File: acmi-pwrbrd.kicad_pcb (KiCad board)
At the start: 2 copper layers, 60 x 140 mm, 25 parts, among them J1 430450402, J10 3-641215-8, J2 430450402, J3 430451202, J4 430451202, J5 430450402

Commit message: Finish routing
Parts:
- removed J10: 3-641215-8, myparts:TE_3-641215-8
- added J6: 39289108, myparts:MOLEX_39289108, F.Cu at (196.5, 124.2)
- added J7: 430451202, myparts:CONN_SD-43045-001_12_MOL, F.Cu at (157.6, 83.2)
- D3: value GREEN -> ~
- moved J5 29.9 mm to (157.6, 55.2)
- moved MT1 25.0 mm to (155.0, 40.0)
- moved MT2 25.0 mm to (205.0, 40.0)
- moved J1 2.56 mm to (157.6, 158.0)
- moved J2 2.56 mm to (157.6, 175.0)
- moved J3 2.56 mm to (157.6, 111.8)
- moved J4 2.56 mm to (157.6, 140.0)
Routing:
- net +12V: track 0.00 -> 242.9 mm, vias 0 -> 4
- net +15V: track 0.00 -> 208.2 mm, vias 0 -> 3
- net -15V: track 0.00 -> 202.8 mm, vias 0 -> 3
- net -5V: track 0.00 -> 191.1 mm, vias 0 -> 4
- net +5V: track 0.00 -> 182.4 mm, vias 0 -> 2
- net GND: track 0.00 -> 9.47 mm, vias 0 -> 5
- net Net-(D3-A): track 0.00 -> 3.26 mm
- net Net-(D5-A): track 0.00 -> 3.24 mm
- net Net-(D4-K): track 0.00 -> 3.24 mm
- net Net-(D2-A): track 0.00 -> 3.24 mm
- net Net-(D1-K): track 0.00 -> 3.24 mm
- added copper zone on B.Cu, net GND
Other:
- board size 60 x 140 mm -> 60 x 165 mm
- board text added: "ACMI-2 Power Distribution Board"
- board text added: "J. Mead 2-24-25 Rev 1"

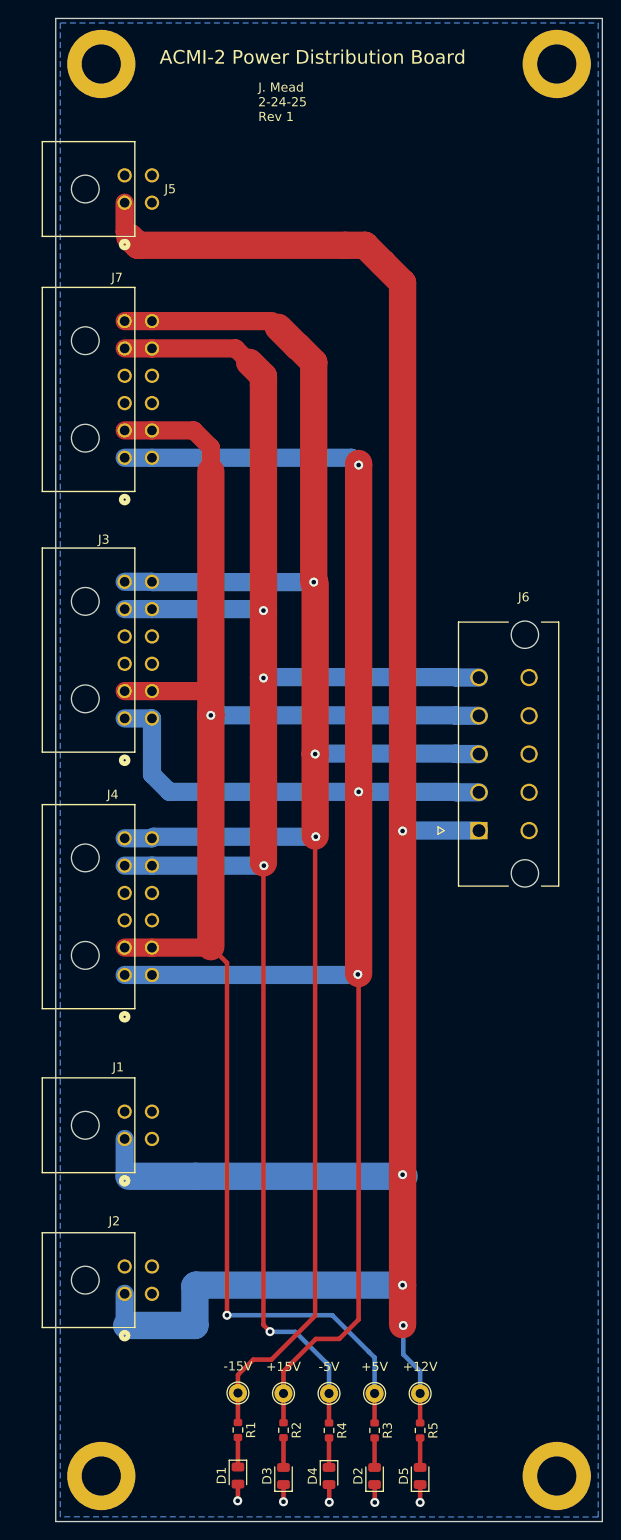
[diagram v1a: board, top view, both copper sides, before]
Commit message: Added 12VB, testpoints, cable harness
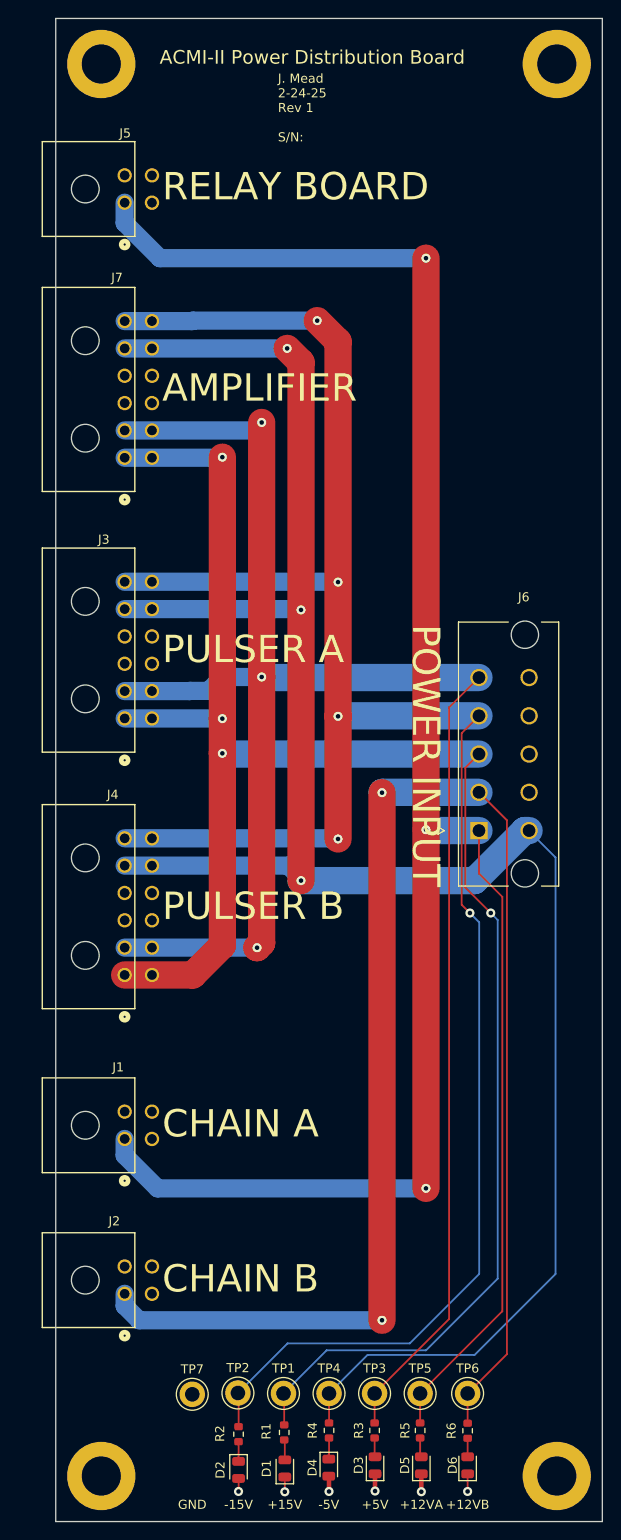
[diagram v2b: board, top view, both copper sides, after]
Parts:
- added D6: ~, LED_SMD:LED_0805_2012Metric, F.Cu at (195.2, 193.8)
- added R6: 895, Resistor_SMD:R_0603_1608Metric, F.Cu at (195.2, 190.0)
- added TP6: +12VB, TestPoint:TestPoint_Keystone_5005-5009_Compact, F.Cu at (195.2, 185.9)
- added TP7: GND, TestPoint:TestPoint_Keystone_5005-5009_Compact, F.Cu at (165.0, 186.0)
- TP1, TP2, TP3, TP4: footprint TestPoint:TestPoint_THTPad_D2.0mm_Drill1.0mm -> TestPoint:TestPoint_Keystone_5005-5009_Compact
- TP5: value +12V -> +12VA; footprint TestPoint:TestPoint_THTPad_D2.0mm_Drill1.0mm -> TestPoint:TestPoint_Keystone_5005-5009_Compact
- moved D2 14.9 mm to (170.1, 194.3), turned to -90 degrees
- moved D3 10.1 mm to (185.1, 193.8)
- moved D1 5.20 mm to (175.1, 194.2), turned to 90 degrees
- moved R1 5.09 mm to (175.1, 190.2)
- moved R2 4.95 mm to (170.1, 190.4)
- moved D5 1.18 mm to (190.1, 193.8)
- moved D4 0.92 mm to (180.0, 194.1)
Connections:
- D1 pad 1: Net-(D1-K) -> GND
- D1 pad 2: GND -> Net-(D1-A)
- D2 pad 1: GND -> Net-(D2-K)
- D2 pad 2: Net-(D2-A) -> GND
- J1 pad 1: +12V -> +12VA
- J2 pad 1: +12V -> +12VB
- J5 pad 1: +12V -> +12VA
- J6 pad 1: +12V -> +12VA
- J6 pad 2: +15V -> +12VB
- J6 pad 3: -15V -> +15V
- J6 pad 4: +5V -> -15V
- J6 pad 5: -5V -> +5V
- J6 pad 6: GND -> -5V
- R1 pad 1: -15V -> +15V
- R1 pad 2: Net-(D1-K) -> Net-(D1-A)
- R2 pad 1: +15V -> -15V
- R2 pad 2: Net-(D3-A) -> Net-(D2-K)
- R3 pad 2: Net-(D2-A) -> Net-(D3-A)
- R5 pad 1: +12V -> +12VA
- TP5 pad 1: +12V -> +12VA
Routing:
- net +12VA: track 0.00 -> 251.1 mm, vias 0 -> 3
- net +12V: track 242.9 -> 0.00 mm, vias 4 -> 0
- net +12VB: track 0.00 -> 171.1 mm, vias 0 -> 2
- net -15V: track 202.8 -> 239.8 mm, vias 3 -> 5
- net -5V: track 191.1 -> 227.1 mm, vias 4 -> 3
- net +5V: track 182.4 -> 213.9 mm, vias 2 -> 3
- net Net-(D2-A): track 3.24 -> 0.00 mm
- net Net-(D1-K): track 3.24 -> 0.00 mm
- net Net-(D2-K): track 0.00 -> 2.16 mm
- net Net-(D1-A): track 0.00 -> 2.13 mm
- net Net-(D6-A): track 0.00 -> 2.03 mm
- net Net-(D3-A): track 3.26 -> 1.76 mm
- net Net-(D5-A): track 3.24 -> 1.93 mm
- net +15V: track 208.2 -> 207.2 mm, vias 3 -> 4
- net GND: track 9.47 -> 10.4 mm, vias 5 -> 6
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- added copper zone on In1.Cu, net GND
- added copper zone on In2.Cu, net GND
- removed copper zone on B.Cu, net GND
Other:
- copper layers 2 -> 4
- board text added: "+12VA"
- board text added: "+12VB"
- board text added: "+15V"
- board text added: "+5V"
- board text added: "-15V"
- board text added: "-5V"
- board text added: "ACMI-II Power Distribution Board"
- board text added: "AMPLIFIER"
- board text added: "CHAIN A"
- board text added: "CHAIN B"
- board text added: "GND"
- board text added: "J. Mead 2-24-25 Rev 1 S/N:"
- board text added: "POWER INPUT"
- board text added: "PULSER A"
- board text added: "PULSER B"
- board text added: "RELAY BOARD"
- board text removed: "ACMI-2 Power Distribution Board"
- board text removed: "J. Mead 2-24-25 Rev 1"

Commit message: Modify silkscreen
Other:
- board text added: "Amplifier"
- board text added: "Chain A"
- board text added: "Chain B"
- board text added: "D/N:"
- board text added: "J. Mead / M. Capotosto 2-24-25 Rev 1"
- board text added: "Power Input"
- board text added: "Pulser A"
- board text added: "Pulser B"
- board text added: "Relay Board"
- board text added: "S/N:"
- board text removed: "AMPLIFIER"
- board text removed: "CHAIN A"
- board text removed: "CHAIN B"
- board text removed: "J. Mead 2-24-25 Rev 1 S/N:"
- board text removed: "POWER INPUT"
- board text removed: "PULSER A"
- board text removed: "PULSER B"
- board text removed: "RELAY BOARD"
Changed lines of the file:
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@@
 		(at 196.46 124.15 -90)
 		(property "Reference" "J6"
-			(at -25.625 -4.915 180)
+			(at 8.875 -6.815 180)
 			(layer "F.SilkS")
 			(effects
@@
 		(embedded_fonts no)
 	)
+	(gr_rect
+		(start 169 47.6)
+		(end 207.35 52.11875)
+		(stroke
+			(width 0.05)
+			(type solid)
+		)
+		(fill yes)
+		(layer "F.SilkS")
+	)
+	(gr_rect
+		(start 191.3 52.7)
+		(end 207.35 57.4125)
+		(stroke
+			(width 0.05)
+			(type solid)
+		)
+		(fill yes)
+		(layer "F.SilkS")
+	)
 	(gr_line
 		(start 150 35)
@@
 		(layer "Edge.Cuts")
 	)
-	(gr_text "AMPLIFIER"
+	(gr_text "Amplifier"
 		(at 161.684 77.318 0)
 		(layer "F.SilkS")
 		(effects
 			(font
-				(size 3 3)
+				(size 2 2)
 				(thickness 0.375)
 			)
@@
 		)
 	)
-	(gr_text "RELAY BOARD"
-		(at 161.684 55.22 0)
+	(gr_text "Relay Board"
+		(at 161.6057 59.054 0)
 		(layer "F.SilkS")
 		(effects
 			(font
-				(size 3 3)
+				(size 2 2)
 				(thickness 0.375)
 			)
@@
 		)
 	)
+	(gr_text "S/N:"
+		(at 186.675 55.675 0)
+		(layer "F.SilkS")
+		(effects
+			(font
+				(size 1 1)
+				(thickness 0.15)
+			)
+			(justify left bottom)
+		)
+	)
+	(gr_text "D/N:"
+		(at 164.55 50.6 0)
+		(layer "F.SilkS")
+		(effects
+			(font
+				(size 1 1)
+				(thickness 0.15)
+			)
+			(justify left bottom)
+		)
+	)
 	(gr_text "+15V"
 		(at 175.146 198.73 0)
@@
 		)
 	)
-	(gr_text "J. Mead\n2-24-25\nRev 1\n\nS/N: "
-		(at 174.384 48.616 0)
+	(gr_text "J. Mead / M. Capotosto\n2-24-25\nRev 1"
+		(at 172.675 47.025 0)
 		(layer "F.SilkS")
 		(effects
@@
 		)
 	)
-	(gr_text "ACMI-II Power Distribution Board"
-		(at 161.4 40.15 0)
+	(gr_text "ACMI-II \nPower Distribution Board"
+		(at 180.2 42.175 0)
 		(layer "F.SilkS")
 		(effects
 			(font
-				(size 1.5 1.5)
-				(thickness 0.15)
+				(size 2 2)
+				(thickness 0.35)
+				(bold yes)
 			)
-			(justify left bottom)
+			(justify bottom)
 		)
 	)
@@
 		)
 	)
-	(gr_text "PULSER B"
+	(gr_text "Pulser B"
 		(at 161.684 134.214 0)
 		(layer "F.SilkS")
 		(effects
 			(font
-				(size 3 3)
+				(size 2 2)
 				(thickness 0.375)
 			)
@@
 		)
 	)
-	(gr_text "PULSER A"
+	(gr_text "Pulser A"
 		(at 161.684 106.02 0)
 		(layer "F.SilkS")
 		(effects
 			(font
-				(size 3 3)
+				(size 2 2)
 				(thickness 0.375)
 			)
@@
 		)
 	)
-	(gr_text "CHAIN A"
+	(gr_text "Chain A"
 		(at 161.684 158.09 0)
 		(layer "F.SilkS")
 		(effects
 			(font
-				(size 3 3)
+				(size 2 2)
 				(thickness 0.375)
 			)
@@
 		)
 	)
-	(gr_text "CHAIN B"
+	(gr_text "Chain B"
 		(at 161.684 175.108 0)
 		(layer "F.SilkS")
 		(effects
 			(font
-				(size 3 3)
+				(size 2 2)
 				(thickness 0.375)
 			)
@@
 		)
 	)
-	(gr_text "POWER INPUT"
-		(at 188.862 115.926 270)
+	(gr_text "Power \nInput"
+		(at 196.025 99.25 0)
 		(layer "F.SilkS")
 		(effects
 			(font
-				(size 3 3)
+				(size 2 2)
 				(thickness 0.375)
 			)
-			(justify bottom)
+			(justify left bottom)
 		)
 	)
